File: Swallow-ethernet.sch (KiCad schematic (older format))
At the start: 30 parts, among them P1 XTAG2, P10 CONN_14, P11 CONN_8, P12 CONN_3, P2 XMP16_TR_Link, P3 TR_Link_Out, P4 Mode_Select, U1 25MHz_ASE_CLK, U14 82R, U15 74LCX257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

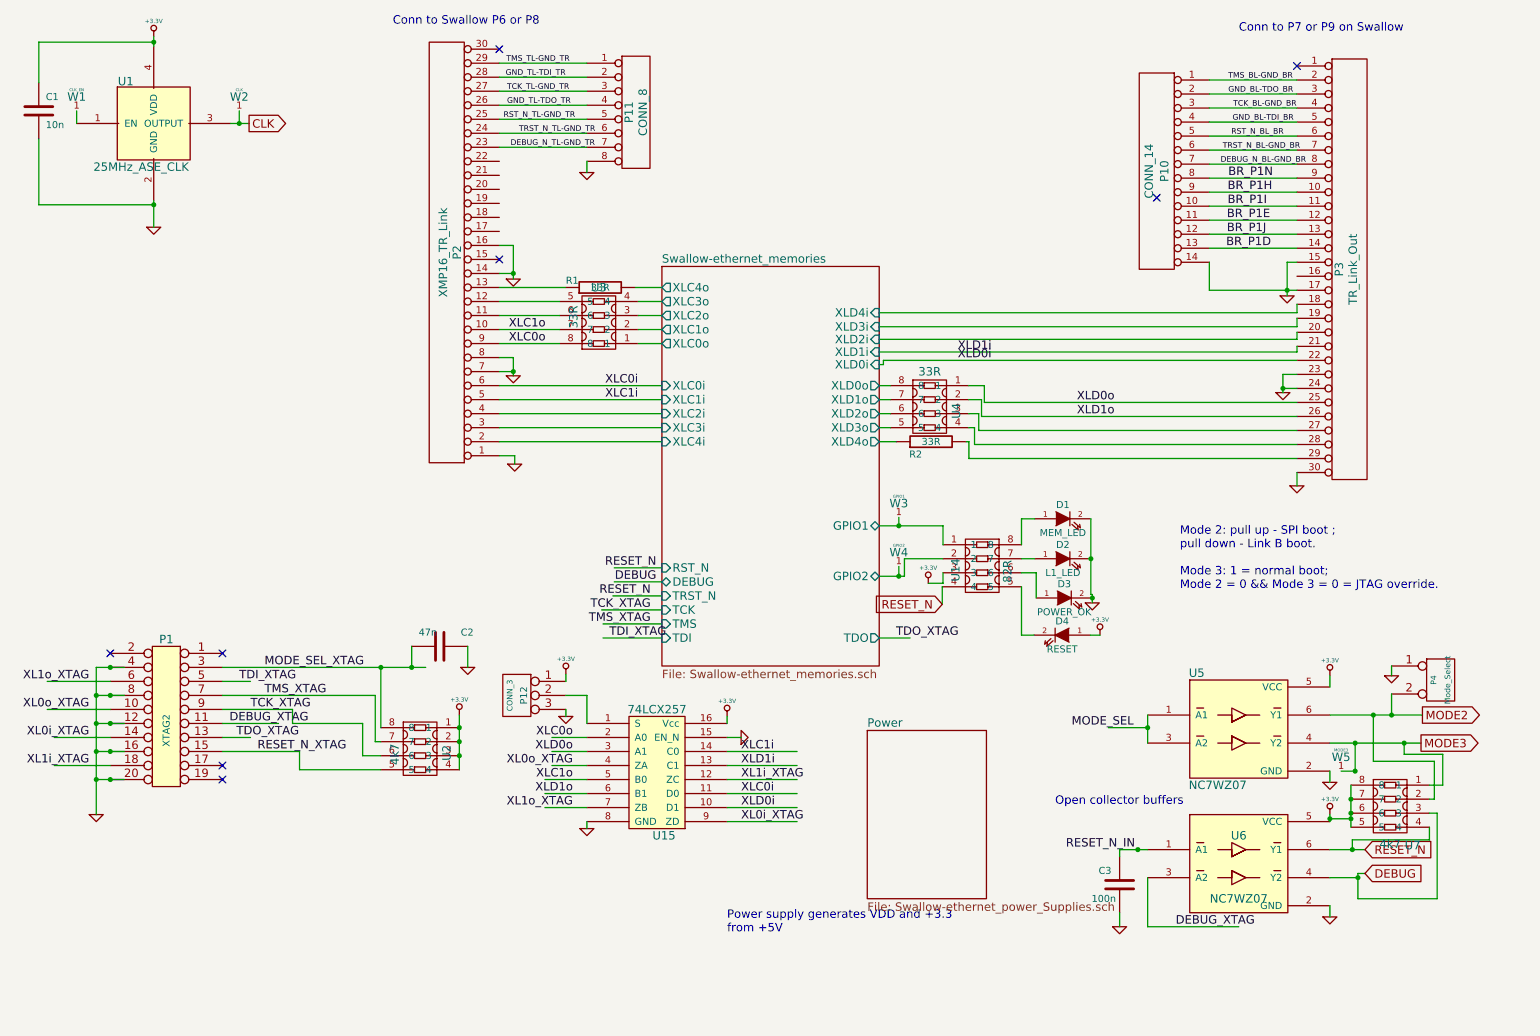
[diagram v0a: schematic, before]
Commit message: Added proper GPIO header and connected a second GPIO to the flash part.
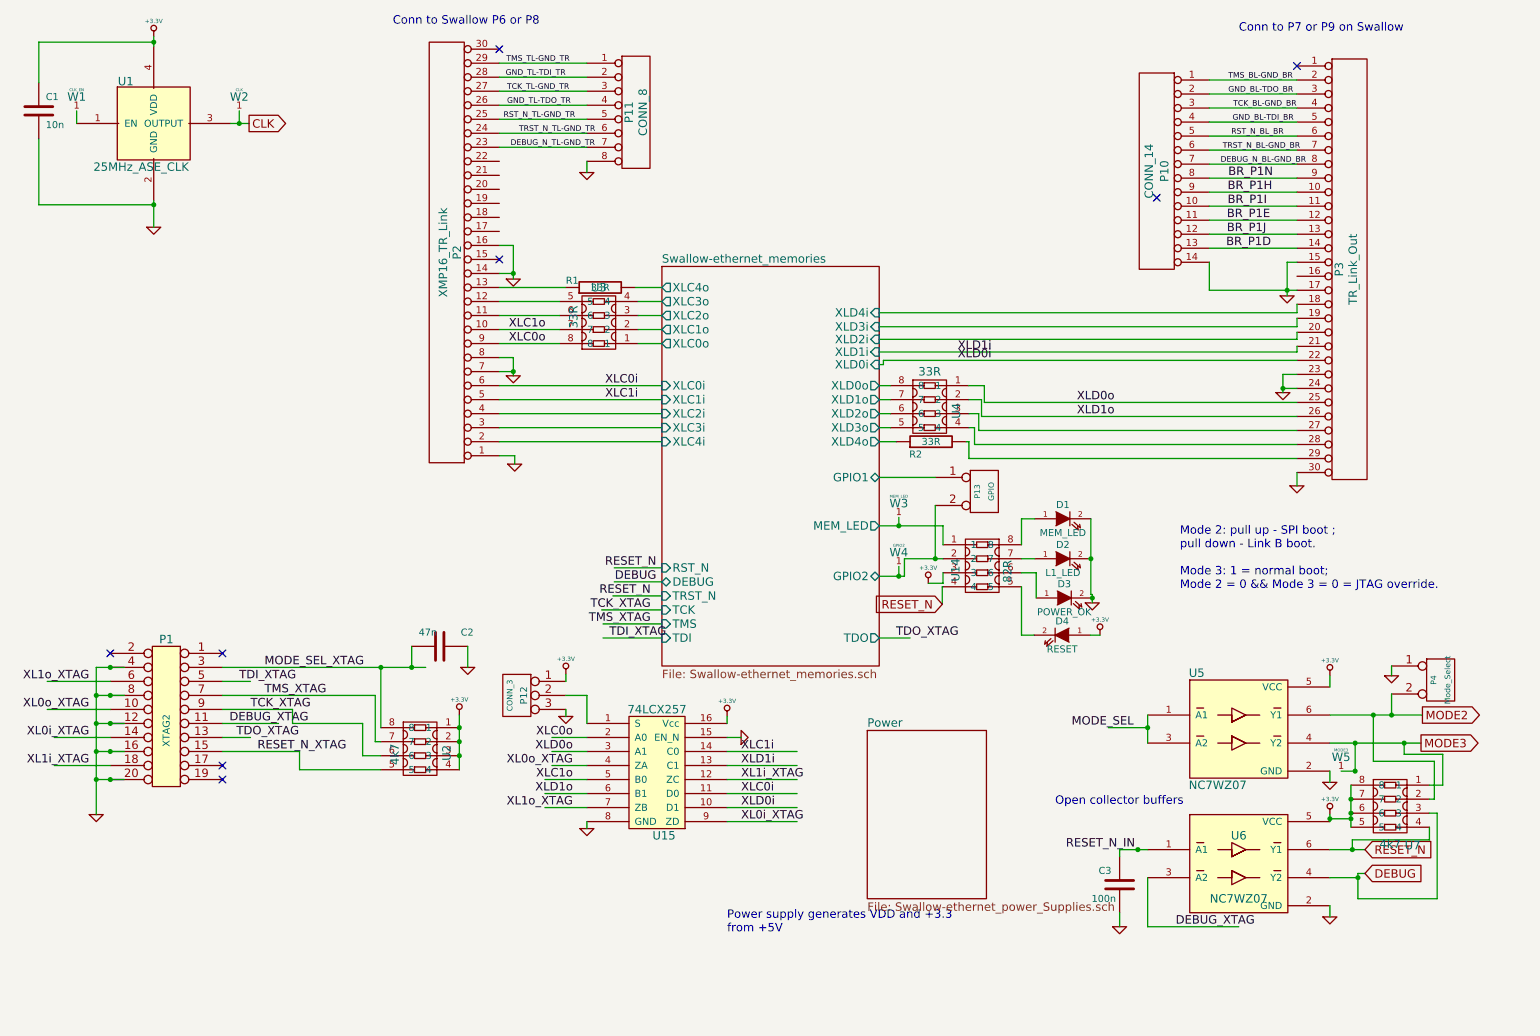
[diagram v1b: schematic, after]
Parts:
- added P13: GPIO, symbol CONN_2
- W3: value GPIO1 -> MEM_LED
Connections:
- wire segments 206 -> 208

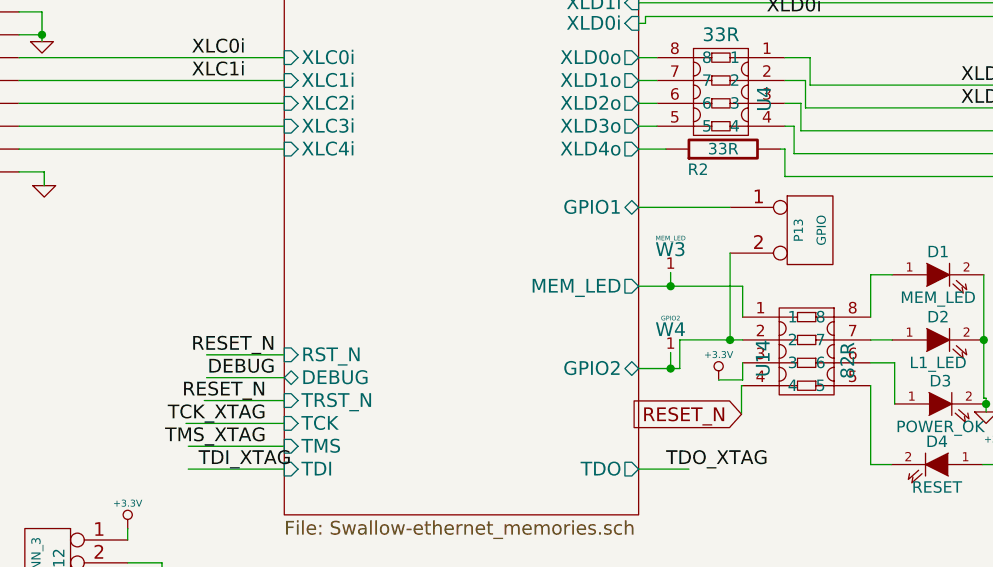
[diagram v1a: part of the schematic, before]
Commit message: Added extra GPIO header from flash pins. Changed LED connection to CLK.
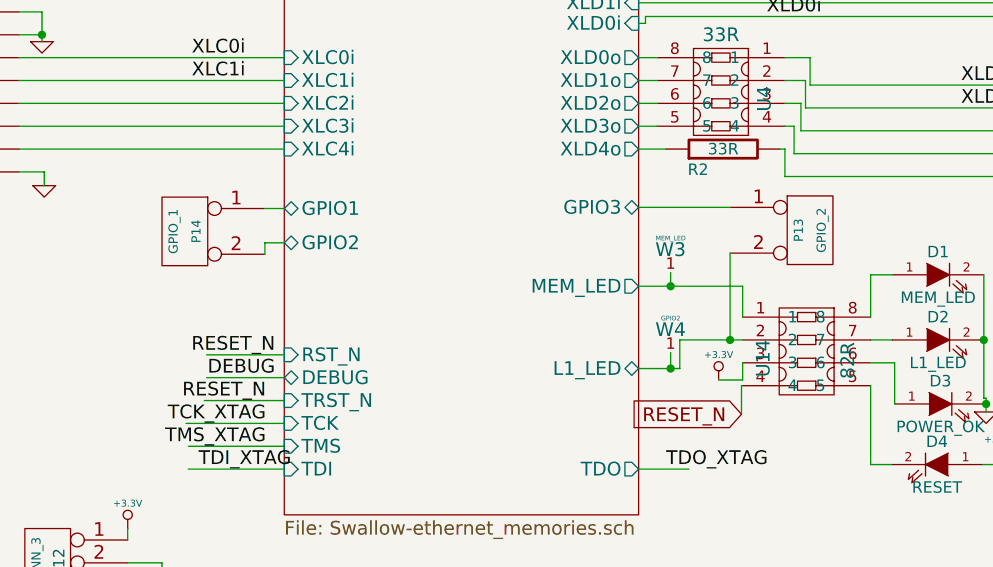
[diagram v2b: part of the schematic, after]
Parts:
- added P14: GPIO_1, symbol CONN_2
- P13: value GPIO -> GPIO_2
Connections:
- wire segments 208 -> 211
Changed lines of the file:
@@
-EESchema Schematic File Version 2  date Mon 08 Oct 2012 20:44:15 BST
+EESchema Schematic File Version 2  date Tue 09 Oct 2012 18:00:45 BST
 LIBS:power
 LIBS:device
@@
 Sheet 1 4
 Title "noname.sch"
-Date "8 oct 2012"
+Date "9 oct 2012"
 Rev ""
 Comp ""
@@
 Comment4 ""
 $EndDescr
+Wire Wire Line
+	5285 4000 5200 4000
+Wire Wire Line
+	5200 4000 5200 4050
 Connection ~ 7235 4425
 Wire Wire Line
@@
 Wire Wire Line
 	4750 5400 4750 5600
+Wire Wire Line
+	5200 3850 5285 3850
+$Comp
+L CONN_2 P14
+U 1 1 50745801
+P 4850 3950
+F 0 "P14" V 4800 3950 40  0000 C CNN
+F 1 "GPIO_1" V 4900 3950 40  0000 C CNN
+	1    4850 3950
+	-1   0    0    -1
+$EndComp
+$Sheet
+S 5285 2340 1550 2850
+U 4F5A2605
+F0 "Swallow-ethernet_memories" 60
+F1 "Swallow-ethernet_memories.sch" 60
+F2 "TDO" O R 6835 4990 60
+F3 "TDI" I L 5285 4990 60
+F4 "TMS" I L 5285 4890 60
+F5 "TCK" I L 5285 4790 60
+F6 "TRST_N" I L 5285 4690 60
+F7 "DEBUG" B L 5285 4590 60
+F8 "RST_N" I L 5285 4490 60
+F9 "XLD0o" O R 6835 3190 60
+F10 "XLD1o" O R 6835 3290 60
+F11 "XLD2o" O R 6835 3390 60
+F12 "XLD3o" O R 6835 3490 60
+F13 "XLD4o" O R 6835 3590 60
+F14 "XLD4i" I R 6835 2670 60
+F15 "XLD3i" I R 6835 2770 60
+F16 "XLD2i" I R 6835 2860 60
+F17 "XLD1i" I R 6835 2950 60
+F18 "XLD0i" I R 6835 3040 60
+F19 "GPIO2" B L 5285 4000 60
+F20 "GPIO1" B L 5285 3850 60
+F21 "XLC0o" O L 5285 2890 60
+F22 "XLC1o" O L 5285 2790 60
+F23 "XLC2o" O L 5285 2690 60
+F24 "XLC3o" O L 5285 2590 60
+F25 "XLC4o" O L 5285 2490 60
+F26 "XLC4i" I L 5285 3590 60
+F27 "XLC3i" I L 5285 3490 60
+F28 "XLC2i" I L 5285 3390 60
+F29 "XLC1i" I L 5285 3290 60
+F30 "XLC0i" I L 5285 3190 60
+F31 "MEM_LED" O R 6835 4190 60
+F32 "GPIO3" B R 6835 3845 60
+F33 "L1_LED" B R 6835 4550 60
+$EndSheet
 $Comp
 L CONN_2 P13
@@
 P 7585 3945
 F 0 "P13" V 7535 3945 40  0000 C CNN
-F 1 "GPIO" V 7635 3945 40  0000 C CNN
+F 1 "GPIO_2" V 7635 3945 40  0000 C CNN
 	1    7585 3945
 	1    0    0    -1
@@
 	1    0    0    -1
 $EndComp
-$Sheet
-S 5285 2340 1550 2850
-U 4F5A2605
-F0 "Swallow-ethernet_memories" 60
-F1 "Swallow-ethernet_memories.sch" 60
-F2 "TDO" O R 6835 4990 60
-F3 "TDI" I L 5285 4990 60
-F4 "TMS" I L 5285 4890 60
-F5 "TCK" I L 5285 4790 60
-F6 "TRST_N" I L 5285 4690 60
-F7 "DEBUG" B L 5285 4590 60
-F8 "RST_N" I L 5285 4490 60
-F9 "XLD0o" O R 6835 3190 60
-F10 "XLD1o" O R 6835 3290 60
-F11 "XLD2o" O R 6835 3390 60
-F12 "XLD3o" O R 6835 3490 60
-F13 "XLD4o" O R 6835 3590 60
-F14 "XLD4i" I R 6835 2670 60
-F15 "XLD3i" I R 6835 2770 60
-F16 "XLD2i" I R 6835 2860 60
-F17 "XLD1i" I R 6835 2950 60
-F18 "XLD0i" I R 6835 3040 60
-F19 "GPIO2" B R 6835 4550 60
-F20 "GPIO1" B R 6835 3845 60
-F21 "XLC0o" O L 5285 2890 60
-F22 "XLC1o" O L 5285 2790 60
-F23 "XLC2o" O L 5285 2690 60
-F24 "XLC3o" O L 5285 2590 60
-F25 "XLC4o" O L 5285 2490 60
-F26 "XLC4i" I L 5285 3590 60
-F27 "XLC3i" I L 5285 3490 60
-F28 "XLC2i" I L 5285 3390 60
-F29 "XLC1i" I L 5285 3290 60
-F30 "XLC0i" I L 5285 3190 60
-F31 "MEM_LED" O R 6835 4190 60
-$EndSheet
 Text Label 2270 5300 0    60   ~ 0
 TDI_XTAG

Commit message: Placed the new GPIO headers. Alpha production candidate.
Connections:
- wire segments 211 -> 212
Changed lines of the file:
@@
-EESchema Schematic File Version 2  date Tue 09 Oct 2012 18:00:45 BST
+EESchema Schematic File Version 2  date Tue 09 Oct 2012 21:50:25 BST
 LIBS:power
 LIBS:device
@@
 $EndDescr
 Wire Wire Line
+	7250 4050 7235 4050
+Wire Wire Line
+	7235 4050 7235 4425
+Wire Wire Line
 	5285 4000 5200 4000
 Wire Wire Line
 	5200 4000 5200 4050
 Connection ~ 7235 4425
-Wire Wire Line
-	7235 4045 7235 4425
-Wire Wire Line
-	7235 3845 6835 3845
 Wire Wire Line
 	4600 5250 4600 5300
@@
 Wire Wire Line
 	5200 3850 5285 3850
-$Comp
-L CONN_2 P14
-U 1 1 50745801
-P 4850 3950
-F 0 "P14" V 4800 3950 40  0000 C CNN
-F 1 "GPIO_1" V 4900 3950 40  0000 C CNN
-	1    4850 3950
-	-1   0    0    -1
-$EndComp
+Wire Wire Line
+	6835 3850 7250 3850
 $Sheet
 S 5285 2340 1550 2850
@@
 F17 "XLD1i" I R 6835 2950 60
 F18 "XLD0i" I R 6835 3040 60
-F19 "GPIO2" B L 5285 4000 60
-F20 "GPIO1" B L 5285 3850 60
+F19 "GPIO2" B L 5285 3850 60
+F20 "GPIO1" B R 6835 3850 60
 F21 "XLC0o" O L 5285 2890 60
 F22 "XLC1o" O L 5285 2790 60
@@
 F30 "XLC0i" I L 5285 3190 60
 F31 "MEM_LED" O R 6835 4190 60
-F32 "GPIO3" B R 6835 3845 60
+F32 "GPIO3" B L 5285 4000 60
 F33 "L1_LED" B R 6835 4550 60
 $EndSheet
 $Comp
+L CONN_2 P14
+U 1 1 50745801
+P 4850 3950
+F 0 "P14" V 4800 3950 40  0000 C CNN
+F 1 "GPIO_1" V 4900 3950 40  0000 C CNN
+	1    4850 3950
+	-1   0    0    -1
+$EndComp
+$Comp
 L CONN_2 P13
 U 1 1 50732BDA
-P 7585 3945
-F 0 "P13" V 7535 3945 40  0000 C CNN
-F 1 "GPIO_2" V 7635 3945 40  0000 C CNN
-	1    7585 3945
+P 7600 3950
+F 0 "P13" V 7550 3950 40  0000 C CNN
+F 1 "GPIO_2" V 7650 3950 40  0000 C CNN
+	1    7600 3950
 	1    0    0    -1
 $EndComp

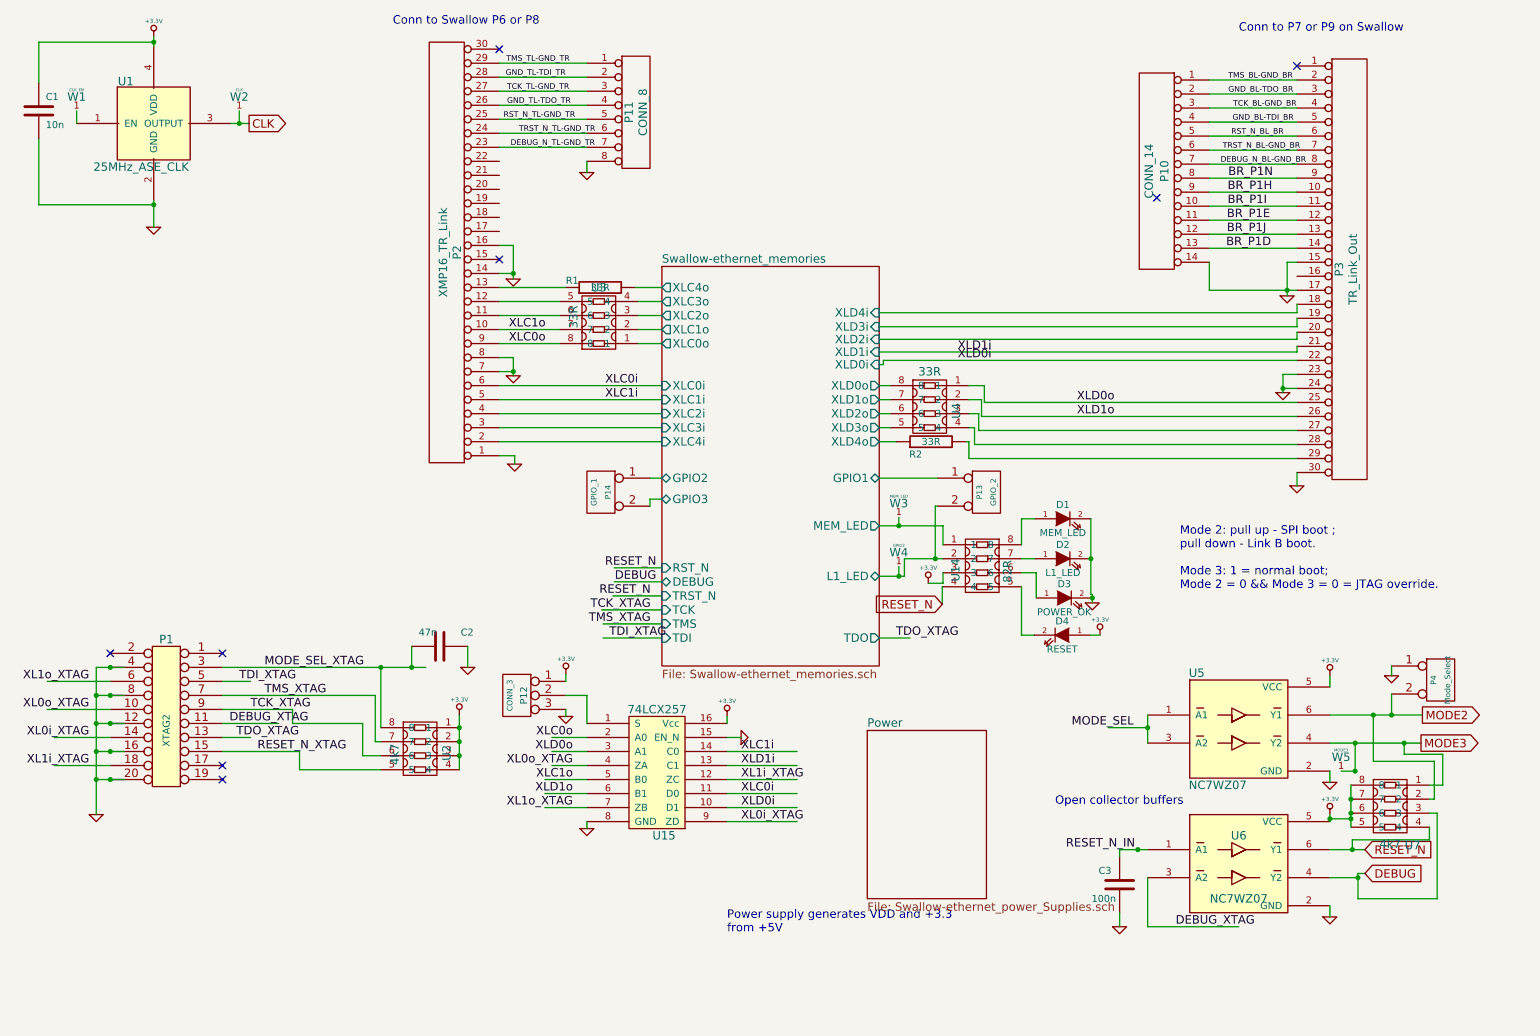
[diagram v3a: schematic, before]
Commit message: Placed four 3mm mounting holes.
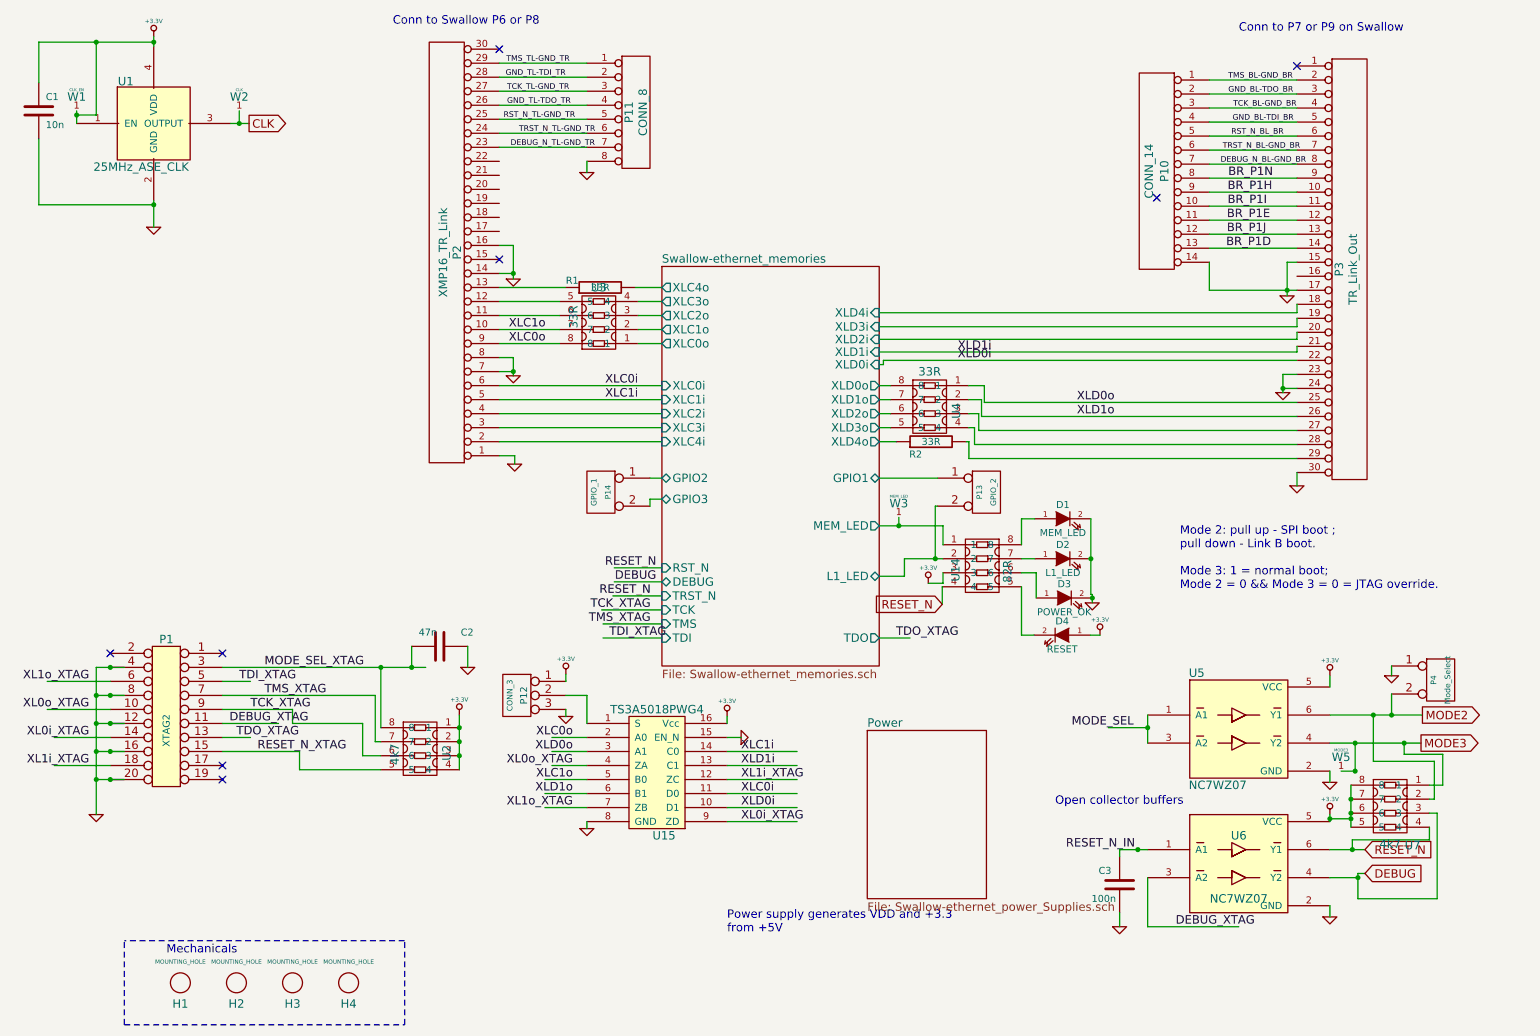
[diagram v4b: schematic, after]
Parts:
- removed W4: GPIO2, TestPad-1mm, symbol TESTPOINT
- added H1, H2, H3, H4: MOUNTING_HOLE, symbol MOUNTING_HOLE
- U15: value 74LCX257 -> TS3A5018PWG4
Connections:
- wire segments 212 -> 213
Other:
- note added: "Mechanicals"
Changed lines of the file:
@@
-EESchema Schematic File Version 2  date Tue 09 Oct 2012 21:50:25 BST
+EESchema Schematic File Version 2  date Wed 10 Oct 2012 18:34:54 BST
 LIBS:power
 LIBS:device
@@
 Sheet 1 4
 Title "noname.sch"
-Date "9 oct 2012"
+Date "10 oct 2012"
 Rev ""
 Comp ""
@@
 Comment4 ""
 $EndDescr
+Connection ~ 1250 740
+Connection ~ 1110 1260
+Wire Wire Line
+	1110 1260 1250 1260
+Wire Wire Line
+	1250 1260 1250 740
 Wire Wire Line
 	7250 4050 7235 4050
@@
 Wire Wire Line
 	10795 5870 10360 5870
-Connection ~ 6975 4550
-Wire Wire Line
-	6975 4480 6975 4550
 Connection ~ 10360 5540
 Wire Wire Line
@@
 Wire Wire Line
 	6835 3850 7250 3850
+Wire Notes Line
+	1450 7750 1450 7150
+Wire Notes Line
+	1450 7750 3450 7750
+Wire Notes Line
+	3450 7750 3450 7150
+Wire Notes Line
+	3450 7150 1450 7150
+Text Notes 1750 7250 0    60   ~ 0
+Mechanicals
+$Comp
+L MOUNTING_HOLE H4
+U 1 1 50749C31
+P 3050 7450
+F 0 "H4" H 3050 7300 60  0000 C CNN
+F 1 "MOUNTING_HOLE" H 3050 7600 30  0000 C CNN
+	1    3050 7450
+	1    0    0    -1
+$EndComp
+$Comp
+L MOUNTING_HOLE H3
+U 1 1 50749C2E
+P 2650 7450
+F 0 "H3" H 2650 7300 60  0000 C CNN
+F 1 "MOUNTING_HOLE" H 2650 7600 30  0000 C CNN
+	1    2650 7450
+	1    0    0    -1
+$EndComp
+$Comp
+L MOUNTING_HOLE H2
+U 1 1 50749C2B
+P 2250 7450
+F 0 "H2" H 2250 7300 60  0000 C CNN
+F 1 "MOUNTING_HOLE" H 2250 7600 30  0000 C CNN
+	1    2250 7450
+	1    0    0    -1
+$EndComp
+$Comp
+L MOUNTING_HOLE H1
+U 1 1 50749C25
+P 1850 7450
+F 0 "H1" H 1850 7300 60  0000 C CNN
+F 1 "MOUNTING_HOLE" H 1850 7600 30  0000 C CNN
+	1    1850 7450
+	1    0    0    -1
+$EndComp
 $Sheet
 S 5285 2340 1550 2850
@@
 P 5300 5950
 F 0 "U15" H 5300 5500 60  0000 C CNN
-F 1 "74LCX257" H 5250 6400 60  0000 C CNN
+F 1 "TS3A5018PWG4" H 5250 6400 60  0000 C CNN
 	1    5300 5950
 	1    0    0    -1
@@
 XLD1i
 $Comp
-L TESTPOINT W4
-U 1 1 4F622646
-P 6975 4330
-F 0 "W4" H 6975 4280 60  0000 C CNN
-F 1 "GPIO2" H 6975 4330 20  0000 C CNN
-F 2 "TestPad-1mm" H 6975 4430 20  0001 C CNN
-	1    6975 4330
-	1    0    0    -1
-$EndComp
-$Comp
 L TESTPOINT W3
